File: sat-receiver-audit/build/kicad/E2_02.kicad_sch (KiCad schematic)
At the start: 66 parts, among them U204 LT3045EMSE#PBF, U205 LT3045EMSE#PBF, U208 TPS2553DBVR-1, U209 TPS2553DBVR-1, U210 TPS2553DBVR-1, U219 TLV3011BIDBVR, U220 TPS3701DDCR

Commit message: Stage 2 integration: CAD and DC_CORE re-freeze from CI run 40094234222; bound-count test and PCB hash lists follow
Co-Authored-By: Claude Opus 5.5 <noreply@anthropic.com>
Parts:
- removed C240: 1uF 50V X7R C2012X7R1H105K125AB, Capacitor_SMD:C_0805_2012Metric, symbol sr_rx_v2_completed:C_C240
- removed C241: 1uF 50V X7R C2012X7R1H105K125AB, Capacitor_SMD:C_0805_2012Metric, symbol sr_rx_v2_completed:C_C241
- removed C242: 1uF 50V X7R C2012X7R1H105K125AB, Capacitor_SMD:C_0805_2012Metric, symbol sr_rx_v2_completed:C_C242
- removed C243: 47uF 50V EEUFR1H470, symbol sr_rx_v2_completed:C_C243
- removed C244: 1uF 50V X7R C2012X7R1H105K125AB, Capacitor_SMD:C_0805_2012Metric, symbol sr_rx_v2_completed:C_C244
- removed C245: 1uF 50V X7R C2012X7R1H105K125AB, Capacitor_SMD:C_0805_2012Metric, symbol sr_rx_v2_completed:C_C245
- removed C246: 1uF 50V X7R C2012X7R1H105K125AB, Capacitor_SMD:C_0805_2012Metric, symbol sr_rx_v2_completed:C_C246
- removed C247: 47uF 50V EEUFR1H470, symbol sr_rx_v2_completed:C_C247
- removed C248: 1uF 50V X7R C2012X7R1H105K125AB, Capacitor_SMD:C_0805_2012Metric, symbol sr_rx_v2_completed:C_C248
- removed C249: 1uF 50V X7R C2012X7R1H105K125AB, Capacitor_SMD:C_0805_2012Metric, symbol sr_rx_v2_completed:C_C249
- removed C250: 1uF 50V X7R C2012X7R1H105K125AB, Capacitor_SMD:C_0805_2012Metric, symbol sr_rx_v2_completed:C_C250
- removed C251: 47uF 50V EEUFR1H470, symbol sr_rx_v2_completed:C_C251
- removed L208: 1uH XAL5030-102MEC, symbol sr_rx_v2_completed:C_L208
- removed L209: 1uH XAL5030-102MEC, symbol sr_rx_v2_completed:C_L209
- removed L210: 1uH XAL5030-102MEC, symbol sr_rx_v2_completed:C_L210
- removed R238: 88.7k 1%, symbol sr_rx_v2_completed:C_R238
- removed R239: 100k 1%, symbol sr_rx_v2_completed:C_R239
- removed R241: 0.200R 0.1% 0.25W Kelvin, symbol sr_rx_v2_completed:C_R241
- removed R242: 0.22R 1% 0.25W, symbol sr_rx_v2_completed:C_R242
- removed R243: 162k 1%, symbol sr_rx_v2_completed:C_R243
- removed R244: 100k 1%, symbol sr_rx_v2_completed:C_R244
- removed R246: 0.200R 0.1% 0.25W Kelvin, symbol sr_rx_v2_completed:C_R246
- removed R247: 0.22R 1% 0.25W, symbol sr_rx_v2_completed:C_R247
- removed R248: RILIM TBD (start 56.2k 1%), symbol sr_rx_v2_completed:C_R248
- removed R249: 100k 1%, symbol sr_rx_v2_completed:C_R249
- removed R251: 0.22R 1% 0.25W, symbol sr_rx_v2_completed:C_R251
- removed TP208: BIAS_CH3, symbol sr_rx_v2_completed:C_TP208
- removed TP209: BIAS_CH4, symbol sr_rx_v2_completed:C_TP209
- removed TP210: VBUS_RTLB, symbol sr_rx_v2_completed:C_TP210
- removed U208: TPS2553DBVR-1, symbol sr_rx_v2_completed:C_U208
- removed U209: TPS2553DBVR-1, symbol sr_rx_v2_completed:C_U209
- removed U210: TPS2553DBVR-1, symbol sr_rx_v2_completed:C_U210
- added C236: 1uF 50V X7R C2012X7R1H105K125AB, Capacitor_SMD:C_0805_2012Metric, symbol sr_rx_v2_completed:C_C236
- added C237: 1uF 50V X7R C2012X7R1H105K125AB, Capacitor_SMD:C_0805_2012Metric, symbol sr_rx_v2_completed:C_C237
- added C238: 1uF 50V X7R C2012X7R1H105K125AB, Capacitor_SMD:C_0805_2012Metric, symbol sr_rx_v2_completed:C_C238
- added C239: 47uF 50V EEUFR1H470, symbol sr_rx_v2_completed:C_C239
- added C2901: 1uF 50V X7R C2012X7R1H105K125AB, Capacitor_SMD:C_0805_2012Metric, symbol sr_rx_v2_completed:C_C2901
- added C2911: 100nF 50V X7R C1608X7R1H104K080AA, Capacitor_SMD:C_0603_1608Metric, symbol sr_rx_v2_completed:C_C2911
- added D2901: BZX84C10-7-F, Package_TO_SOT_SMD:SOT-23, symbol sr_rx_v2_completed:C_D2901
- added L207: 1uH XAL5030-102MEC, symbol sr_rx_v2_completed:C_L207
- added Q2901: DMP6050SSD-13, Package_SO:SOIC-8_3.9x4.9mm_P1.27mm, symbol sr_rx_v2_completed:C_Q2901
- added Q2911: 2N7002, Package_TO_SOT_SMD:SOT-23, symbol sr_rx_v2_completed:C_Q2911
- added R233: 88.7k 1%, symbol sr_rx_v2_completed:C_R233
- added R234: 100k 1%, symbol sr_rx_v2_completed:C_R234
- added R236: 0.200R 0.1% 0.25W Kelvin, symbol sr_rx_v2_completed:C_R236
- added R237: 0.22R 1% 0.25W, symbol sr_rx_v2_completed:C_R237
- added R2901: 220k 1%, Resistor_SMD:R_0603_1608Metric, symbol sr_rx_v2_completed:C_R2901
- added R2911: 4.7k 1% ≥0.25W, Resistor_SMD:R_1210_3225Metric, symbol sr_rx_v2_completed:C_R2911
- added R2921: 4.7k 1%, Resistor_SMD:R_0603_1608Metric, symbol sr_rx_v2_completed:C_R2921
- added TP207: BIAS_CH2, symbol sr_rx_v2_completed:C_TP207
- added TP2901: BIAS_CH2_PORT, symbol sr_rx_v2_completed:C_TP2901
- added U207: TPS2553DBVR-1, symbol sr_rx_v2_completed:C_U207
- R227: value 22.5k 0.1% -> 21.5k 0.1% 25ppm; footprint (none) -> Resistor_SMD:R_0603_1608Metric
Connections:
- net GND: now also C236.2, C237.2, C238.2, C239.2 (-), C2901.2, Q2911.2 (S), R233.2, R234.2, R2921.2, U207.2 (GND)
- net LNA4V5: now also C236.1, U207.1 (IN)
- new net BIAS_CH2: C238.1, L207.2, Q2901.7 (D1), Q2901.8 (D1), R237.1, R2921.1, TP207.1 (TP)
- new net BIAS_CH2_DAMP: C239.1 (+), R237.2
- new net BIAS_CH2_PORT: C2901.1, Q2901.5 (D2), Q2901.6 (D2), TP2901.1 (TP)
- new net E2_BLK2_G: C2911.2, D2901.1 (A), Q2901.2 (G1), Q2901.4 (G2), R2901.2, R2911.1
- new net E2_BLK2_S: C2911.1, D2901.3 (K), Q2901.1 (S1), Q2901.3 (S2), R2901.1
- new net E2_BLK2_SINK: Q2911.3 (D), R2911.2
- new net E2_LNA2_SHUNT: C237.1, L207.1, R236.2
- new net E2_LNA2_SW: R236.1, U207.6 (OUT)
- new net E2_U207_ILIM: R233.1, U207.5 (ILIM)
- new net EN_LNA2: Q2911.1 (G), R234.1, U207.3 (EN)
- new net FAULT_LNA2: U207.4 (FAULT)
- no-connect marks 3 -> 4
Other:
- note added: "E2 - Захищені рейки, LNA і моніторинг струму (2/5)"
- note added: "LNA: канал 2"
- note added: "N-E2-03 — примітка — STACK §5.3 (DC-sense); §8.1 HF-10"
- note added: "Q2901–Q2903 (DMP6050SSD-13) — двобічні блокувальні елементи ±30 V воріт E4-06 між захищеним вузлом E2 і портом E4; закриті при низькому EN_LNA2/EN_LNA3/EN_BONI. Позначення 2900–2999 — задокументований розширений діапазон E2 (R-E2-21). Ворота: E4-06 (повільний і швидкий hot-plug на зібраному порту)."
- note added: "v2.1, рішення власника (R-E2-18): R227 21.5k задає LNA4V5 4.30V (4.208…4.392V). Запас на папері: LAB5 min 4.80V (5V−4%) − 3.2A×29.8mΩ L101 − 1A×9.4mΩ L205 = 4.695V на E2_LNA_IN, тобто 0.395V над VSET: +135mV проти типового dropout 260mV (500mA на ІС), +45mV проти 350mV max при 25°C, −55mV проти 450mV max у повному діапазоні температур — ще до F102 і з'єднання E1→E2 (кожні 10mΩ — −32mV при 3.2A). 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"
- note removed: "E2 - Захищені рейки, LNA і моніторинг струму (2/4)"
- note removed: "E2-03 — OPEN, блокує випуск — STACK §5.1 (VBUS RTL-B, BONI13V8); §8 (струми; TPS2553DBVR-1 п. 3); §8.1 RF-2, HF-8/RF-5"
- note removed: "LNA: канал 3"
- note removed: "LNA: канал 4"
- note removed: "N-E2-01 — примітка — STACK §5.1 (VBUS RTL-B); §8 (TPS2553DBVR-1 п. 3)"
- note removed: "R248 = RILIM TBD (старт 56.2k 1%, ≈0.47 A ном.). STACK не задає номінал для VBUS RTL-B, лише правило: RILIM = 1.5–2× виміряного струму. Ворота: E2-03 (20 холодних і теплих пусків, пусковий струм до deglitch 5 ms)."
- note removed: "RTL-B: комутований VBUS"
- note removed: "Запас напруги пари LT3045 на 4.5V на папері від'ємний: LAB5 min 4.80V (5V−4%) − 3.2A×29.8mΩ L101 − 1A×9.4mΩ L205 = 4.695V на E2_LNA_IN (4.684V за моделлю міді 55°C) проти 4.5V + 0.26V типового dropout при 500mA = 4.76V, тобто −65mV ще до спаду на запобіжнику й PCB. Пара в dropout при LAB5 нижче ≈4.865V, PSRR втрачено. Розподіл струму й температура не підтверджені. Сума індивідуальних номінальних 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"
- note removed: "Остаточні ILIM і пускові струми RTL-B, Lime, LNB, Boni та LaNA WB потребують натурних вимірів; ємність riser і комерційних модулів не опублікована. Поріг OVLO Boni (R263/R264, стартовий розрахунок 112k/10.0k) STACK §5.1 вимагає перерахувати для 13.8 V; на стенді його не перевірено. Ворота (стенд): FNB58/INA228/INA3221: 20 холодних і теплих пусків, струми стримінгу, КЗ і SOA. Установити ILIM 1.5–2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"
- title: E2 - Захищені рейки, LNA і моніторинг струму (2/4) -> E2 - Захищені рейки, LNA і моніторинг струму (2/5)
- moved on the sheet: C227, C229, C230, C231, C286, C287, C288, C290, C292, R225, R226, R286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

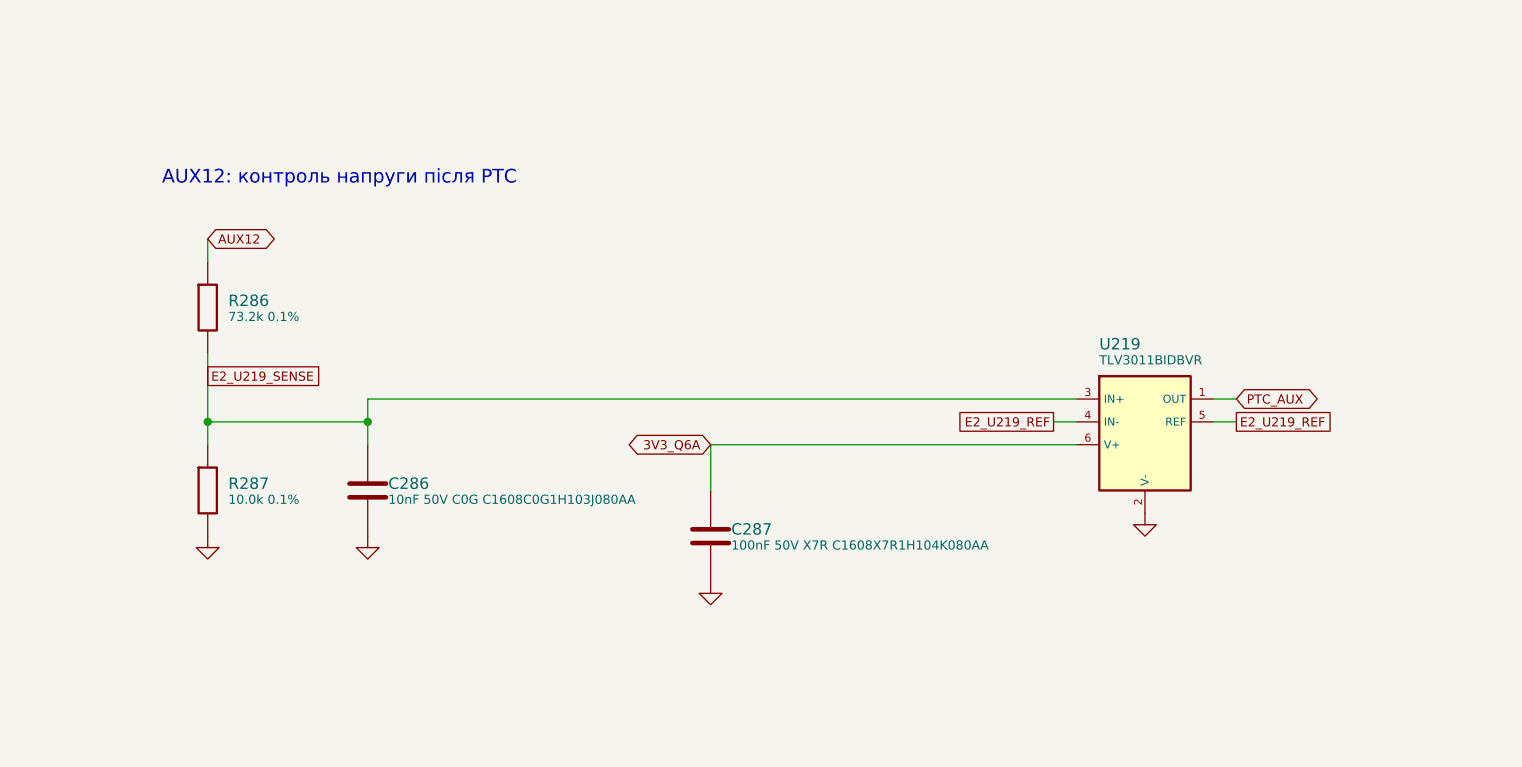
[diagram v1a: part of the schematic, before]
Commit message: GENERATED: CAD, documents, verification reports, DC_CORE re-freeze and module-lab inventory for f3f57e8
Applied unchanged from the cad-regenerated artifact of CI run 40109759054
(workflow_dispatch, refreeze_pcb=true, KiCad 10.0.7): schematics, SVG, PDF,
netlist, OPEN_ITEMS.md, COMPLETION.md, verification/{electrical-invariants,
independent-netlist-review,netlist,pcb-review,pcb-prototype-review,
pdf-export,validation}, pcb/generated and the re-frozen DC_CORE starter and
routed prototype with their pinned hashes. Inputs: the stage 3A merge,
design/E2.json (PICO-2 text) and STACK.md (2.7 row).

deployment/module_lab/inventory.json: source_snapshots only, from
deployment/module_lab/refresh_inventory.py (E2.json and STACK.md bytes).

Co-Authored-By: Claude Opus 5.5 <noreply@anthropic.com>
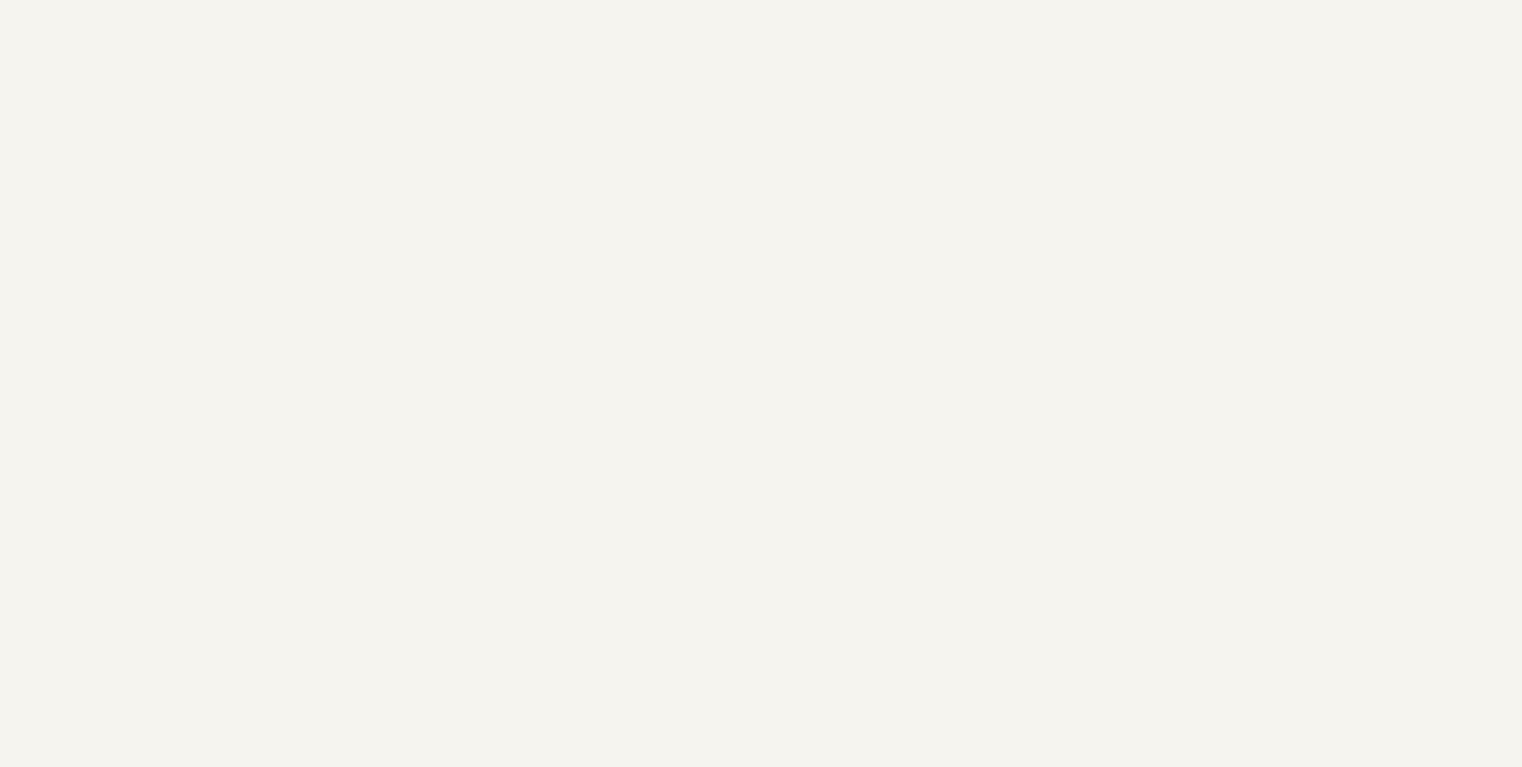
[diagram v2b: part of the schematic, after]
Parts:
- removed C286: 10nF 50V C0G C1608C0G1H103J080AA, Capacitor_SMD:C_0603_1608Metric, symbol sr_rx_v2_completed:C_C286
- removed C287: 100nF 50V X7R C1608X7R1H104K080AA, Capacitor_SMD:C_0603_1608Metric, symbol sr_rx_v2_completed:C_C287
- removed R286: 73.2k 0.1%, symbol sr_rx_v2_completed:C_R286
- removed R287: 10.0k 0.1%, symbol sr_rx_v2_completed:C_R287
- removed U219: TLV3011BIDBVR, symbol sr_rx_v2_completed:C_U219
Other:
- note removed: "AUX12: контроль напруги після PTC"
